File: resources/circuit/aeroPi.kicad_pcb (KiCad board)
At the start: 2 copper layers, 65 x 56.5 mm, 80 parts, among them J1 CONN_COAXIAL, J2 Screw_Terminal_1x12, P1 CONN_01X02, P2 CONN_01X02, P3 Raspberry_Pi_+_Conn, Q1 BSS138, U1 LM3489, U10 Airspeed, U11 Static Pressure, U12 MAP Pressure, U2 CAT24C32HU4I-GT3, U3 FDC5614P, U4 LM1117IMPX-ADJ, U5 DMMT5401, U6 FGPMMOPA6H, U7 MPU-9250, U8 MCP3008BIS, U9 MCP3008BIS

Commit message: Work on schematic & PCB
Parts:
- moved R8 1.81 mm to (137.4, 115.6)
- moved R7 1.52 mm to (130.5, 116.5)
- moved R9 1.44 mm to (137.4, 118.3)
- moved U8 1.02 mm to (133.2, 86.1)
- moved C14 1.02 mm to (122.6, 87.9)
- moved C15 1.02 mm to (122.6, 97.4)
- moved C16 1.02 mm to (122.6, 107.0)
- moved C17 1.02 mm to (120.1, 85.2)
- moved R16 1.02 mm to (121.8, 85.2)
- moved R17 1.02 mm to (121.8, 94.9)
- moved R18 1.02 mm to (121.8, 104.3)
- moved R19 1.02 mm to (122.6, 82.9)
- moved R21 1.02 mm to (125.0, 86.0)
- moved R22 1.02 mm to (122.6, 92.6)
- moved R23 1.02 mm to (123.5, 94.9)
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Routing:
- net GND: track 132.3 -> 70.1 mm, vias 9 -> 7
- net /+3.3V: track 31.2 -> 85.1 mm, vias 3 -> 1
- net Net-(U11-Pad5): track 39.0 -> 0.00 mm
- net Net-(R8-Pad1): track 102.3 -> 91.5 mm, vias 3 -> 5
- net Net-(C5-Pad2): track 5.06 -> 8.77 mm
- net Net-(JP1-Pad1): track 20.3 -> 23.2 mm
- net /SCLK: track 16.2 -> 15.1 mm
- net /MCP0_ADDR: track 11.1 -> 10.5 mm
- net +24V: track 32.4 -> 31.7 mm

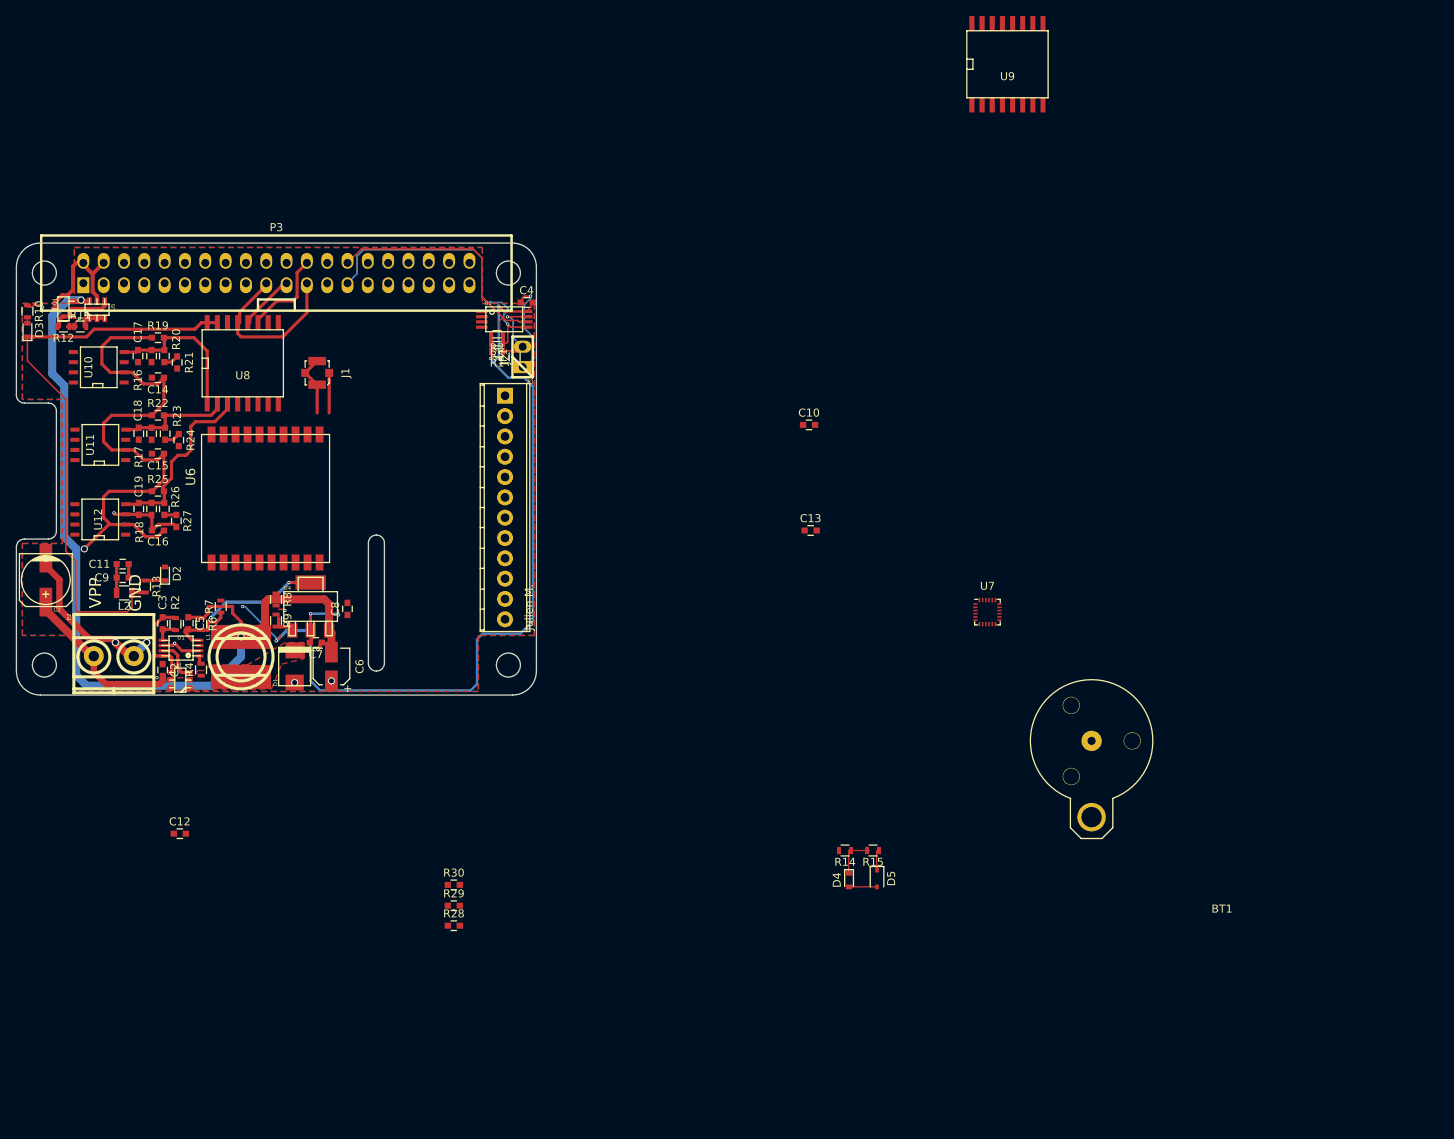
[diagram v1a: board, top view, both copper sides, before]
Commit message: Clear PCB network + clean schematic
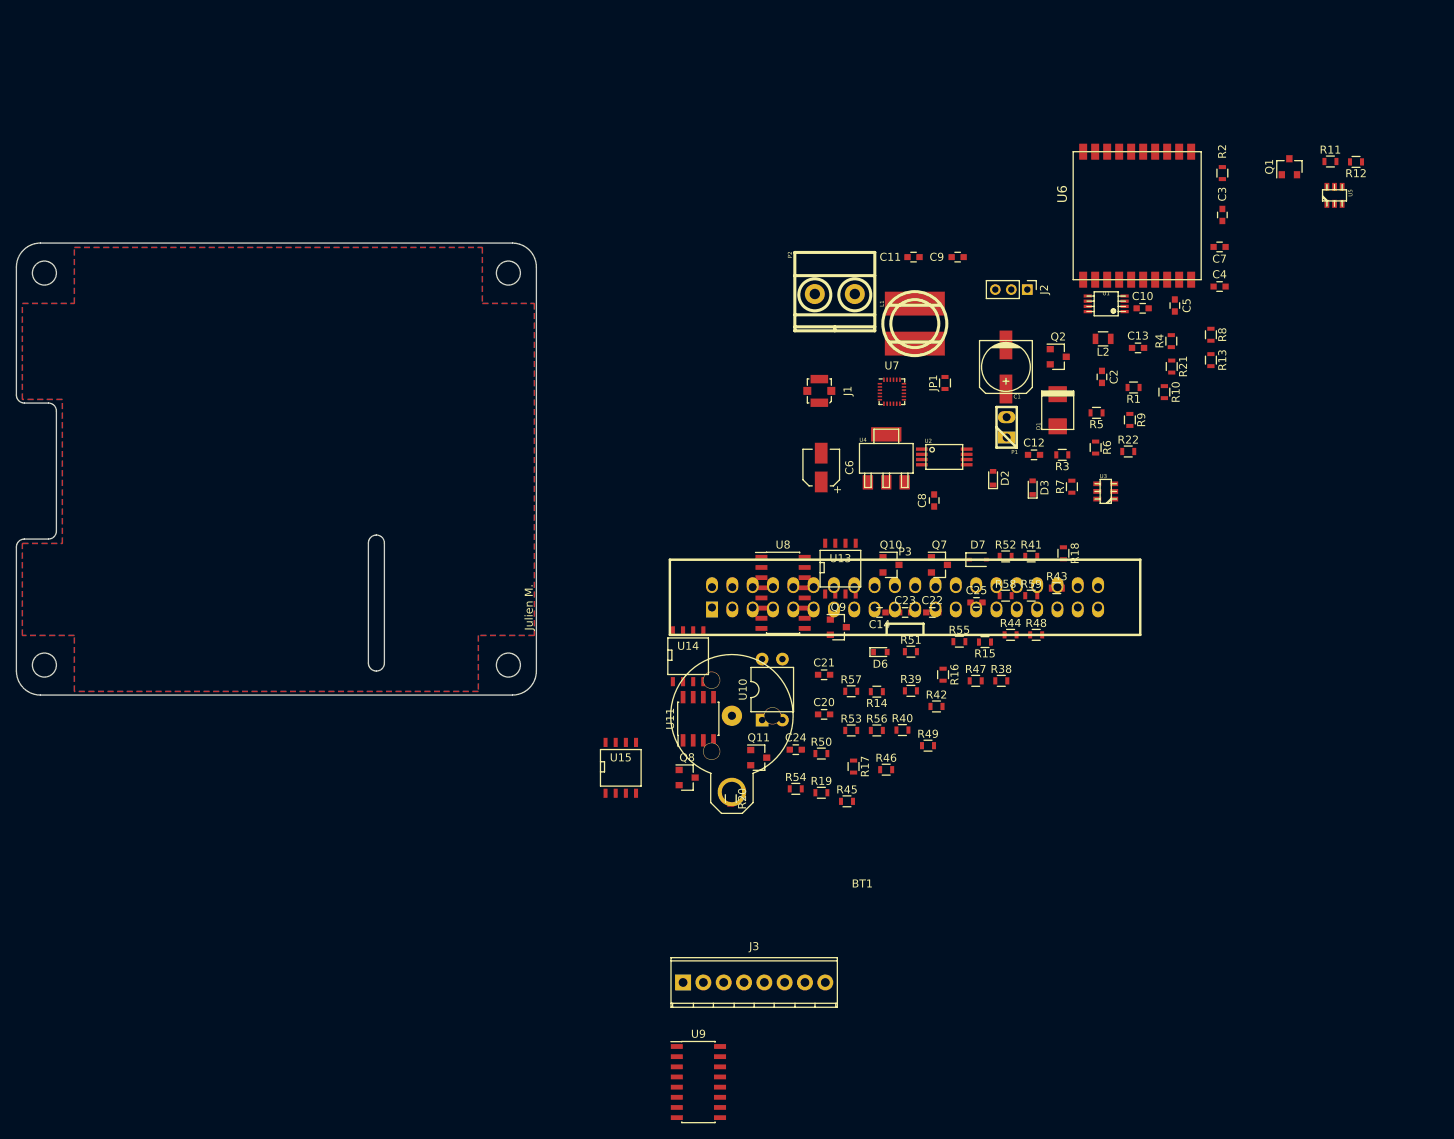
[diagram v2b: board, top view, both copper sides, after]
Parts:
- removed C15, C16: 100n, Capacitors_SMD:C_0603
- removed C17, C18, C19: 47p, Capacitors_SMD:C_0603
- removed D4: Diode, Diodes_SMD:D_0603
- removed D5: 3.3V, Diodes_SMD:D_SOD-323
- removed R23, R24, R25, R26, R27: 1k, Capacitors_SMD:C_0603
- removed R28, R29, R30: 220, Capacitors_SMD:C_0603
- removed U12: MAP Pressure, SMD_Packages:SOIC-8-N
- added C20: 0.1u, Capacitors_SMD:C_0603, F.Cu at (205.9, 130.0)
- added C21: 0.1u, Capacitors_SMD:C_0603, F.Cu at (205.9, 125.0)
- added C22: 0.1u, Capacitors_SMD:C_0603, F.Cu at (219.4, 117.2)
- added C23: 47p, Capacitors_SMD:C_0603, F.Cu at (216.0, 117.2)
- added C24: 47p, Capacitors_SMD:C_0603, F.Cu at (202.3, 134.4)
- added C25: 47p, Capacitors_SMD:C_0603, F.Cu at (224.9, 116.0)
- added D6: Diode, Diodes_SMD:D_0603, F.Cu at (212.9, 122.2)
- added D7: 5.6V, Diodes_SMD:D_SOD-323, F.Cu at (225.1, 110.6)
- added J3: Screw_Terminal_1x08, Connectors_Terminal_Blocks:TerminalBlock_Pheonix_MPT-2.54mm_8pol, F.Cu at (188.3, 163.5)
- added Q10: BSS138, TO_SOT_Packages_SMD:SOT-23, F.Cu at (214.2, 111.3)
- added Q11: BSS138, TO_SOT_Packages_SMD:SOT-23, F.Cu at (197.7, 135.4)
- added Q2: BSS138, TO_SOT_Packages_SMD:SOT-23, F.Cu at (235.2, 85.3)
- added Q7: BSS138, TO_SOT_Packages_SMD:SOT-23, F.Cu at (220.3, 111.3)
- added Q8: BSS138, TO_SOT_Packages_SMD:SOT-23, F.Cu at (188.8, 137.9)
- added Q9: BSS138, TO_SOT_Packages_SMD:SOT-23, F.Cu at (207.7, 119.1)
- added R38: 51k, Resistors_SMD:R_0603, F.Cu at (228.0, 125.8)
- added R39: 51k, Resistors_SMD:R_0603, F.Cu at (216.7, 127.0)
- added R40: 51k, Resistors_SMD:R_0603, F.Cu at (215.7, 131.9)
- added R41: 1k, Resistors_SMD:R_0603, F.Cu at (231.8, 110.2)
- added R42: 2k, Resistors_SMD:R_0603, F.Cu at (219.9, 129.0)
- added R43: 1k, Resistors_SMD:R_0603, F.Cu at (235.0, 114.2)
- added R44: 2k, Resistors_SMD:R_0603, F.Cu at (229.2, 120.0)
- added R45: 1k, Resistors_SMD:R_0603, F.Cu at (208.7, 140.9)
- added R46: 2k, Resistors_SMD:R_0603, F.Cu at (213.6, 136.9)
- added R47: 220, Resistors_SMD:R_0603, F.Cu at (224.8, 125.8)
- added R48: 220, Resistors_SMD:R_0603, F.Cu at (232.4, 120.0)
- added R49: 220, Resistors_SMD:R_0603, F.Cu at (218.9, 133.9)
- added R50: 10k, Resistors_SMD:R_0603, F.Cu at (205.5, 134.9)
- added R51: 10k, Resistors_SMD:R_0603, F.Cu at (216.7, 122.1)
- added R52: 10k, Resistors_SMD:R_0603, F.Cu at (228.6, 110.2)
- added R53: 10k, Resistors_SMD:R_0603, F.Cu at (209.3, 132.0)
- added R54: 10k, Resistors_SMD:R_0603, F.Cu at (202.3, 139.3)
- added R55: 10k, Resistors_SMD:R_0603, F.Cu at (222.8, 120.9)
- added R56: 10k, Resistors_SMD:R_0603, F.Cu at (212.5, 132.0)
- added R57: 10k, Resistors_SMD:R_0603, F.Cu at (209.3, 127.1)
- added R58: 10k, Resistors_SMD:R_0603, F.Cu at (228.6, 115.1)
- added R59: 10k, Resistors_SMD:R_0603, F.Cu at (231.8, 115.1)
- added U13: Airspeed, SMD_Packages:SOIC-8-N, F.Cu at (207.9, 111.8)
- added U14: Static Pressure, SMD_Packages:SOIC-8-N, F.Cu at (188.9, 122.7)
- added U15: MAP Pressure, SMD_Packages:SOIC-8-N, F.Cu at (180.5, 136.7)
- C10: value 10nF -> 10n
- C12, C13: value 0.1uF -> 0.1u
- C14: value 100n -> 22n
- J2: value Screw_Terminal_1x12 -> CONN_01X03; footprint Connectors_Terminal_Blocks:TerminalBlock_Pheonix_MPT-2.54mm_12pol -> Pin_Headers:Pin_Header_Straight_1x03_Pitch2.00mm
- Q1: footprint w_smd_trans:sot23 -> TO_SOT_Packages_SMD:SOT-23
- R14: value 10k -> 47k
- R15: value 100k -> 100
- R16: value 51k -> 10k; footprint Capacitors_SMD:C_0603 -> Resistors_SMD:R_0603
- R17, R18: value 51k -> 100k; footprint Capacitors_SMD:C_0603 -> Resistors_SMD:R_0603
- R19, R21, R22: value 1k -> 10k; footprint Capacitors_SMD:C_0603 -> Resistors_SMD:R_0603
- R20: value 1k -> 220; footprint Capacitors_SMD:C_0603 -> Resistors_SMD:R_0603
- U10: value Airspeed -> LTV-817; footprint SMD_Packages:SOIC-8-N -> Housings_DIP:DIP-4_W7.62mm
- U11: value Static Pressure -> LM358; footprint SMD_Packages:SOIC-8-N -> Housings_SOIC:SOIC-8_3.9x4.9mm_Pitch1.27mm
- U8, U9: value MCP3008BIS -> MCP3008; footprint SMD_Packages:SO-16-L -> Housings_SOIC:SOIC-16_3.9x9.9mm_Pitch1.27mm
- moved R12 162.9 mm to (272.4, 60.9)
- moved R11 157.6 mm to (269.2, 60.9)
- moved U5 155.3 mm to (269.7, 65.1)
- moved Q1 154.3 mm to (264.0, 61.5)
- moved R2 142.5 mm to (255.7, 62.3)
- moved R10 142.5 mm to (248.4, 89.7)
- moved C3 142.0 mm to (255.7, 67.6)
- moved R13 136.2 mm to (254.2, 85.7)
- moved U9 133.0 mm to (190.2, 175.9)
- moved C5 129.6 mm to (249.7, 78.9)
- moved R4 128.1 mm to (249.3, 83.3)
- moved D3 127.2 mm to (232.0, 101.6)
- moved L2 126.4 mm to (240.8, 83.0)
- moved R21 124.3 mm to (249.3, 86.5)
- moved U1 123.4 mm to (241.1, 78.7)
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- renumbered REF** to M0, REF** to M1, REF** to M2, REF** to M3
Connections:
- C14 pad 1: /+5V -> Net-(C14-Pad1)
- J2 pad 2: Net-(J2-Pad2) -> GND
- J2 pad 3: Net-(J2-Pad3) -> /+5V
- P3 pad 19: /MISO -> /MOSI
- P3 pad 21: /MOSI -> /MISO
- P3 pad 24: /MCP0_ADDR -> /Analog Sensors/MCP0_ADDR
- P3 pad 26: /MCP1_ADDR -> /Analog Sensors/MCP1_ADDR
- P3 pad 29: /MPU0_ADDR -> Net-(P3-Pad29)
- P3 pad 3: Net-(P3-Pad3) -> /I2C_SDA
- P3 pad 31: /TACH -> /Analog Sensors/TACH
- P3 pad 32: Net-(P3-Pad32) -> /Fuel_Flow
- P3 pad 5: Net-(P3-Pad5) -> /I2C_SCLK
- P3 pad 7: /MPU0_INT -> Net-(P3-Pad7)
- R14 pad 1: Net-(D4-Pad1) -> Net-(C14-Pad1)
- R14 pad 2: /TACH_IN -> Net-(D7-Pad1)
- R15 pad 1: /TACH -> /Analog Sensors/TACH
- R15 pad 2: Net-(D4-Pad1) -> /+3.3V
- R16 pad 1: /ASI -> Net-(D6-Pad1)
- R16 pad 2: GND -> /Analog Sensors/Tachometer
- R17 pad 1: /BARO -> Net-(D7-Pad1)
- R17 pad 2: GND -> Net-(D6-Pad1)
- R18 pad 1: /MAP -> Net-(R18-Pad1)
- R18 pad 2: GND -> /+5V
- R19 pad 1: /+5V -> GND
- R19 pad 2: /ASI -> Net-(R18-Pad1)
- R20 pad 1: /ASI -> Net-(R20-Pad1)
- R21 pad 1: Net-(R20-Pad2) -> /+5V
- R21 pad 2: GND -> Net-(J2-Pad1)
- R22 pad 1: /+5V -> /+3.3V
- R22 pad 2: /BARO -> /Fuel_Flow
- U10 pad 1: Net-(U10-Pad1) -> Net-(R20-Pad2)
- U10 pad 2: /+5V -> GND
- U10 pad 4: /ASI -> /Analog Sensors/TACH
- U11 pad 2: /+5V -> Net-(U11-Pad1)
- U11 pad 3: GND -> Net-(C14-Pad1)
- U11 pad 4: /BARO -> GND
- U11 pad 5: Net-(U11-Pad5) -> Net-(U11-Pad1)
- U11 pad 6: Net-(U11-Pad6) -> Net-(R18-Pad1)
- U11 pad 7: Net-(U11-Pad7) -> Net-(R20-Pad1)
- U11 pad 8: Net-(U11-Pad8) -> /+5V
- U7 pad 12: /MPU0_INT -> Net-(U7-Pad12)
- U7 pad 22: /MPU0_ADDR -> Net-(U7-Pad22)
- U7 pad 23: /SCLK -> /I2C_SCLK
- U7 pad 24: /MOSI -> /I2C_SDA
- U7 pad 9: /MISO -> Net-(U7-Pad9)
- U8 pad 1: /ASI -> /Analog Sensors/ASI
- U8 pad 10: /MCP0_ADDR -> /Analog Sensors/MCP0H
- U8 pad 11: /MOSI -> /Analog Sensors/MOSIH
- U8 pad 12: /MISO -> /Analog Sensors/MISOH
- U8 pad 13: /SCLK -> /Analog Sensors/SCLKH
- U8 pad 15: /+3.3V -> /+5V
- U8 pad 16: /+3.3V -> /+5V
- U8 pad 2: /BARO -> /Analog Sensors/BARO
- U8 pad 3: /MAP -> /Analog Sensors/MAP
- U8 pad 4: /OilPressure -> /Analog Sensors/OilPressure
- U8 pad 5: /OilTemp -> /Analog Sensors/OilTemp
- U8 pad 6: /CHT -> /Analog Sensors/CHT
- U8 pad 7: Net-(U8-Pad7) -> /Analog Sensors/CurrentMeter
- U8 pad 8: Net-(U8-Pad8) -> /Analog Sensors/VoltageMeter
- U9 pad 10: /MCP1_ADDR -> /Analog Sensors/MCP1H
- U9 pad 11: /MOSI -> /Analog Sensors/MOSIH
- U9 pad 12: /MISO -> /Analog Sensors/MISOH
- U9 pad 13: /SCLK -> /Analog Sensors/SCLKH
- U9 pad 15: /+3.3V -> /+5V
- U9 pad 16: /+3.3V -> /+5V
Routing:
- net /+5V: track 179.2 -> 0.00 mm, vias 4 -> 0
- net Net-(R8-Pad1): track 91.5 -> 0.00 mm, vias 5 -> 0
- net /+3.3V: track 85.1 -> 0.00 mm, vias 1 -> 0
- net GND: track 70.1 -> 0.00 mm, vias 7 -> 0
- net Net-(P3-Pad27): track 37.3 -> 0.00 mm, vias 1 -> 0
- net +24V: track 31.7 -> 0.00 mm
- net Net-(P3-Pad28): track 31.3 -> 0.00 mm
- net Net-(JP1-Pad1): track 23.2 -> 0.00 mm, vias 3 -> 0
- net /MAP: track 22.7 -> 0.00 mm
- net /ASI: track 19.4 -> 0.00 mm
- net /Back Power Protection/5V_MCU: track 15.5 -> 0.00 mm
- net /SCLK: track 15.1 -> 0.00 mm
- net (no net): track 14.3 -> 0.00 mm, vias 3 -> 0
- net /BARO: track 14.3 -> 0.00 mm
- net /MCP0_ADDR: track 10.5 -> 0.00 mm
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- removed copper zone on F.Cu, net Net-(D1-Pad2)
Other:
- board text removed: "GND"
- board text removed: "VPP"

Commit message: Work on circuit & PCB
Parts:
- removed C2: 0.1uf, Capacitors_SMD:C_0603
- removed C22: 0.1u, Capacitors_SMD:C_0603
- removed C25: 47p, Capacitors_SMD:C_0603
- removed C6: 10uf/6.3V, Capacitors_SMD:CP_Elec_4x5.3
- removed C8: 1uf, Capacitors_SMD:C_0603
- removed D1: DIODESCH, w_smd_diode:do214aa
- removed D3: LED, Diodes_SMD:D_0603
- removed D6: Diode, Diodes_SMD:D_0603
- removed D7: 5.6V, Diodes_SMD:D_SOD-323
- removed L1: 22uH, w_smd_inductors:inductor_smd_8x5mm
- removed Q10, Q11, Q7, Q8, Q9: BSS138, TO_SOT_Packages_SMD:SOT-23
- removed R10: 360, Resistors_SMD:R_0603
- removed R18: 100k, Resistors_SMD:R_0603
- removed R2: 24k, Resistors_SMD:R_0603
- removed R38, R39, R40: 51k, Resistors_SMD:R_0603
- removed R4: 270, Resistors_SMD:R_0603
- removed R41, R43, R45: 1k, Resistors_SMD:R_0603
- removed R42, R44, R46: 2k, Resistors_SMD:R_0603
- removed R47, R48, R49: 220, Resistors_SMD:R_0603
- removed R50, R51, R52, R53, R54, R55, R56, R57, R58, R59, R7: 10k, Resistors_SMD:R_0603
- removed R6: 30k, Resistors_SMD:R_0603
- removed R8: 390, Resistors_SMD:R_0603
- removed R9: 240, Resistors_SMD:R_0603
- removed U10: LTV-817, Housings_DIP:DIP-4_W7.62mm
- removed U13: Airspeed, SMD_Packages:SOIC-8-N
- removed U14: Static Pressure, SMD_Packages:SOIC-8-N
- removed U15: MAP Pressure, SMD_Packages:SOIC-8-N
- removed U4: LM1117IMPX-ADJ, w_smd_trans:sot223
- added C16: 1u, Capacitors_SMD:C_0603, F.Cu at (168.0, 109.1)
- added C17: 0.01u, Capacitors_SMD:C_0603, F.Cu at (159.7, 124.1)
- added C19: 0.1u, Capacitors_SMD:C_0603, F.Cu at (153.8, 98.9)
- added D4: Diode, Diodes_SMD:D_0603, F.Cu at (162.7, 105.6)
- added D5: 5.6V, Diodes_SMD:D_SOD-323, F.Cu at (167.3, 101.7)
- added J4: CONN_01X03, Pin_Headers:Pin_Header_Straight_1x03_Pitch2.54mm, F.Cu at (152.8, 114.5)
- added J5: CONN_01X03, Pin_Headers:Pin_Header_Straight_1x03_Pitch2.54mm, F.Cu at (152.8, 118.8)
- added P4: CONN_01X02, Pin_Headers:Pin_Header_Straight_1x02_Pitch2.54mm, F.Cu at (108.8, 83.4)
- added Q3: BSS138, TO_SOT_Packages_SMD:SOT-23, F.Cu at (157.0, 90.8)
- added Q4: BSS138, TO_SOT_Packages_SMD:SOT-23, F.Cu at (167.6, 89.2)
- added Q5: BSS138, TO_SOT_Packages_SMD:SOT-23, F.Cu at (138.1, 81.2)
- added R23: 220, Resistors_SMD:R_0603, F.Cu at (152.6, 104.1)
- added R24: 10k, Resistors_SMD:R_0603, F.Cu at (154.1, 91.6)
- added R25: 10k, Resistors_SMD:R_0603, F.Cu at (159.7, 90.6)
- added R26: 100k, Resistors_SMD:R_0603, F.Cu at (164.4, 90.9)
- added R27: 10k, Resistors_SMD:R_0603, F.Cu at (161.7, 96.1)
- added R28: 10k, Resistors_SMD:R_0603, F.Cu at (164.4, 89.2)
- added R29: 10k, Resistors_SMD:R_0603, F.Cu at (164.4, 87.5)
- added R30: 10k, Resistors_SMD:R_0603, F.Cu at (138.4, 83.9)
- added R31: 10k, Resistors_SMD:R_0603, F.Cu at (135.4, 81.4)
- added U12: LM358, Housings_SOIC:SOIC-8_3.9x4.9mm_Pitch1.27mm, F.Cu at (165.5, 95.9)
- C1: value 50uf/50v -> 100n; footprint w_smd_cap:c_elec_6.3x7.7 -> Capacitors_SMD:C_0603
- C14: value 22n -> 1u
- C20: value 0.1u -> 0.01u
- C21: value 0.1u -> 470p
- C24: value 47p -> 22n
- C3: value 1nf -> 10u
- C5: value 0.1uf -> 100n
- C7: value 0.1uf -> 10u
- J2: footprint Pin_Headers:Pin_Header_Straight_1x03_Pitch2.00mm -> Pin_Headers:Pin_Header_Straight_1x03_Pitch2.54mm
- J3: value Screw_Terminal_1x08 -> CONN_01X04; footprint Connectors_Terminal_Blocks:TerminalBlock_Pheonix_MPT-2.54mm_8pol -> Pin_Headers:Pin_Header_Straight_1x04_Pitch2.54mm
- P1: footprint w_pin_strip:pin_strip_2 -> Pin_Headers:Pin_Header_Straight_1x02_Pitch2.54mm
- P2: footprint w_conn_mkds:mkds_1,5-2 -> Pin_Headers:Pin_Header_Straight_1x02_Pitch2.54mm
- P3: footprint w_conn_strip:vasch_strip_20x2 -> w_pin_strip:pin_socket_20x2
- R14: value 47k -> 10k
- R15: value 100 -> 220
- R16: value 10k -> 100k
- R17: value 100k -> 47k
- R19: value 10k -> 51k
- U1: value LM3489 -> MIC5219-3.3BM5; footprint w_smd_dil:msoic-8 -> TO_SOT_Packages_SMD:SOT-23-5
- U11: value LM358 -> MAP Pressure; footprint Housings_SOIC:SOIC-8_3.9x4.9mm_Pitch1.27mm -> SMD_Packages:SOIC-8-N
- U3: value FDC5614P -> BME280; footprint w_smd_trans:sot23-6 -> aeroPi:BME280
- U8: value MCP3008 -> Airspeed; footprint Housings_SOIC:SOIC-16_3.9x9.9mm_Pitch1.27mm -> SMD_Packages:SOIC-8-N
- U9: value MCP3008 -> ADS7828; footprint Housings_SOIC:SOIC-16_3.9x9.9mm_Pitch1.27mm -> Housings_SSOP:TSSOP-16_4.4x5mm_Pitch0.65mm
- moved R11 161.7 mm to (109.5, 86.3), turned to 180 degrees
- moved R12 161.6 mm to (112.8, 87.0)
- moved U5 158.3 mm to (112.5, 84.4), turned to 270 degrees
- moved Q1 151.7 mm to (113.6, 81.0)
- moved C3 143.9 mm to (114.4, 95.0), turned to 180 degrees
- moved C7 143.9 mm to (114.4, 100.6)
- moved C5 133.2 mm to (118.5, 101.9), turned to 180 degrees
- moved R13 129.3 mm to (126.2, 103.8), turned to 90 degrees
- moved C10 128.8 mm to (118.5, 99.4), turned to 180 degrees
- moved U1 128.4 mm to (114.2, 97.8), turned to 270 degrees
- moved C13 124.3 mm to (121.8, 99.4), turned to 180 degrees
- moved U3 119.5 mm to (121.6, 102.9), turned to 0 degrees
- moved L2 117.2 mm to (124.9, 100.8), turned to 90 degrees
- moved U6 113.8 mm to (138.1, 106.6), turned to 0 degrees
- moved C1 111.4 mm to (118.5, 103.4), turned to 180 degrees
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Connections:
- C1 pad 1: +24V -> /+3.3V
- C14 pad 1: Net-(C14-Pad1) -> /+5V
- C21 pad 1: /+5V -> /ASI
- C23 pad 1: /Analog Sensors/ASI -> /MAP
- C24 pad 1: /Analog Sensors/BARO -> Net-(C24-Pad1)
- C3 pad 1: +24V -> /+5V
- C3 pad 2: Net-(C3-Pad2) -> GND
- C5 pad 1: /+5V -> /+3.3V
- C5 pad 2: Net-(C5-Pad2) -> GND
- J3 pad 1: /Analog Sensors/OilPressure -> /Tachometer
- J3 pad 2: /Analog Sensors/OilTemp -> /CHT
- J3 pad 3: /Analog Sensors/CHT -> /OilTemp
- J3 pad 4: /Analog Sensors/Tachometer -> /OilPressure
- P2 pad 1: +24V -> GND
- P2 pad 2: GND -> /+5V
- P3 pad 1: Net-(P3-Pad1) -> (no net)
- P3 pad 11: Net-(P3-Pad11) -> (no net)
- P3 pad 12: Net-(P3-Pad12) -> (no net)
- P3 pad 13: Net-(P3-Pad13) -> (no net)
- P3 pad 15: Net-(P3-Pad15) -> (no net)
- P3 pad 16: Net-(P3-Pad16) -> (no net)
- P3 pad 17: Net-(P3-Pad17) -> (no net)
- P3 pad 18: Net-(P3-Pad18) -> (no net)
- P3 pad 19: /MOSI -> (no net)
- P3 pad 21: /MISO -> (no net)
- P3 pad 22: Net-(P3-Pad22) -> /Fuel_Flow
- P3 pad 23: /SCLK -> (no net)
- P3 pad 24: /Analog Sensors/MCP0_ADDR -> (no net)
- P3 pad 26: /Analog Sensors/MCP1_ADDR -> (no net)
- P3 pad 29: Net-(P3-Pad29) -> /1PPS
- P3 pad 31: /Analog Sensors/TACH -> (no net)
- P3 pad 32: /Fuel_Flow -> (no net)
- P3 pad 33: Net-(P3-Pad33) -> (no net)
- P3 pad 35: Net-(P3-Pad35) -> (no net)
- P3 pad 36: Net-(P3-Pad36) -> (no net)
- P3 pad 37: Net-(P3-Pad37) -> (no net)
- P3 pad 40: Net-(P3-Pad40) -> (no net)
- P3 pad 7: Net-(P3-Pad7) -> /Tach
- Q1 pad 3: /+5V -> /+5VRpi
- Q2 pad 2: /Fuel_Flow -> /I2C_SDA
- Q2 pad 3: Net-(J2-Pad1) -> Net-(Q2-Pad3)
- R14 pad 1: Net-(C14-Pad1) -> Net-(D4-Pad1)
- R14 pad 2: Net-(D7-Pad1) -> /Tachometer
- R15 pad 1: /Analog Sensors/TACH -> /CHT
- R15 pad 2: /+3.3V -> /+5V
- R16 pad 2: /Analog Sensors/Tachometer -> Net-(D4-Pad1)
- R17 pad 1: Net-(D7-Pad1) -> Net-(C24-Pad1)
- R19 pad 1: GND -> /MAP
- R19 pad 2: Net-(R18-Pad1) -> GND
- R20 pad 1: Net-(R20-Pad1) -> /OilTemp
- R20 pad 2: Net-(R20-Pad2) -> /+5V
- R21 pad 2: Net-(J2-Pad1) -> Net-(Q2-Pad3)
- R22 pad 2: /Fuel_Flow -> /I2C_SDA
- U1 pad 1: Net-(R4-Pad2) -> /+5V
- U1 pad 3: Net-(U1-Pad3) -> /+5V
- U1 pad 4: Net-(C5-Pad2) -> (no net)
- U1 pad 5: Net-(C3-Pad2) -> /+3.3V
- U11 pad 1: Net-(U11-Pad1) -> (no net)
- U11 pad 2: Net-(U11-Pad1) -> /+5V
- U11 pad 3: Net-(C14-Pad1) -> GND
- U11 pad 4: GND -> /MAP
- U11 pad 5: Net-(U11-Pad1) -> (no net)
- U11 pad 6: Net-(R18-Pad1) -> (no net)
- U11 pad 7: Net-(R20-Pad1) -> (no net)
- U11 pad 8: /+5V -> (no net)
- U3 pad 1: Net-(D1-Pad2) -> GND
- U3 pad 2: Net-(D1-Pad2) -> /+3.3V
- U3 pad 3: Net-(U1-Pad7) -> /I2C_SDA
- U3 pad 4: +24V -> /I2C_SCLK
- U3 pad 5: Net-(D1-Pad2) -> GND
- U3 pad 6: Net-(D1-Pad2) -> /+3.3V
- U5 pad 6: /+5V -> /+5VRpi
- U6 pad 13: Net-(U6-Pad13) -> /1PPS
- U6 pad 14: Net-(U6-Pad14) -> (no net)
- U6 pad 15: Net-(U6-Pad15) -> (no net)
- U6 pad 16: Net-(U6-Pad16) -> (no net)
- U6 pad 17: Net-(U6-Pad17) -> (no net)
- U6 pad 18: Net-(U6-Pad18) -> (no net)
- U6 pad 2: Net-(U6-Pad2) -> (no net)
- U6 pad 20: Net-(U6-Pad20) -> (no net)
- U6 pad 6: Net-(U6-Pad6) -> (no net)
- U6 pad 7: Net-(U6-Pad7) -> (no net)
- U7 pad 11: Net-(U7-Pad11) -> (no net)
- U7 pad 12: Net-(U7-Pad12) -> (no net)
- U7 pad 22: Net-(U7-Pad22) -> /+3.3V
- U7 pad 6: Net-(U7-Pad6) -> (no net)
- U7 pad 7: Net-(U7-Pad7) -> (no net)
- U7 pad 9: Net-(U7-Pad9) -> GND
- U8 pad 1: /Analog Sensors/ASI -> (no net)
- U8 pad 2: /Analog Sensors/BARO -> /+5V
- U8 pad 3: /Analog Sensors/MAP -> GND
- U8 pad 4: /Analog Sensors/OilPressure -> /ASI
- U8 pad 5: /Analog Sensors/OilTemp -> (no net)
- U8 pad 6: /Analog Sensors/CHT -> (no net)
- U8 pad 7: /Analog Sensors/CurrentMeter -> (no net)
- U8 pad 8: /Analog Sensors/VoltageMeter -> (no net)
- U9 pad 1: Net-(U9-Pad1) -> /OilPressure
- U9 pad 10: /Analog Sensors/MCP1H -> /+5V
- U9 pad 11: /Analog Sensors/MOSIH -> GND
- U9 pad 12: /Analog Sensors/MISOH -> GND
- U9 pad 13: /Analog Sensors/SCLKH -> GND
- U9 pad 14: GND -> Net-(Q3-Pad3)
- U9 pad 15: /+5V -> Net-(Q2-Pad3)
- U9 pad 2: Net-(U9-Pad2) -> /OilTemp
- U9 pad 3: Net-(U9-Pad3) -> /CHT
- U9 pad 4: Net-(U9-Pad4) -> /CurrentMeter
- U9 pad 5: Net-(U9-Pad5) -> /VoltageMeter
- U9 pad 6: Net-(U9-Pad6) -> /ASI
- U9 pad 7: Net-(U9-Pad7) -> /MAP
- U9 pad 8: Net-(U9-Pad8) -> (no net)
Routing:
- net /+5V: track 0.00 -> 168.1 mm, vias 0 -> 2
- net /+3.3V: track 0.00 -> 133.4 mm, vias 0 -> 4
- net /I2C_SDA: track 0.00 -> 82.0 mm, vias 0 -> 3
- net /I2C_SCLK: track 0.00 -> 75.5 mm, vias 0 -> 3
- net /Tach: track 0.00 -> 55.8 mm, vias 0 -> 2
- net /TXD: track 0.00 -> 50.6 mm, vias 0 -> 2
- net /RXD: track 0.00 -> 44.1 mm, vias 0 -> 2
- net /1PPS: track 0.00 -> 36.1 mm, vias 0 -> 1
- net Net-(P3-Pad28): track 0.00 -> 26.6 mm, vias 0 -> 2
- net Net-(P3-Pad27): track 0.00 -> 25.1 mm, vias 0 -> 2
- net /ASI: track 0.00 -> 23.1 mm
- net /VBACKUP: track 0.00 -> 21.6 mm
- net /VoltageMeter: track 0.00 -> 16.7 mm, vias 0 -> 1
- net /Back Power Protection/5V_MCU: track 0.00 -> 14.1 mm
- net /Fuel_Flow: track 0.00 -> 13.8 mm, vias 0 -> 1
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- added copper zone on F.Cu, net Net-(C11-Pad1)
- added copper zone on F.Cu, net Net-(R11-Pad1)
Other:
- board text added: "+5V"
- board text added: "+5V Gnd Sig Flow meter"
- board text added: "+5V Rpi"
- board text added: "+5V Sig Gnd"
- board text added: "+Vcc 8V - 40V"
- board text added: "A. meter"
- board text added: "CD System"
- board text added: "Display Power +5V Gnd"
- board text added: "GND"
- board text added: "Gnd"
- board text added: "Oil Press Oil Temp CHT Tach"
- board text added: "V. meter"
- board text removed: "CERN OHL V1.2"
- board text removed: "Julien M."
